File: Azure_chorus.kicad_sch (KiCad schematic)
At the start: 90 parts, among them Q1 2N5088, Q2 2N5088, Q3 2N5088, Q4 2N5088, Q5 2N5088, SW1 SW_DPDT_x2, U1 RC4558, U2 MN3207, U3 MN3102, U4 TL022

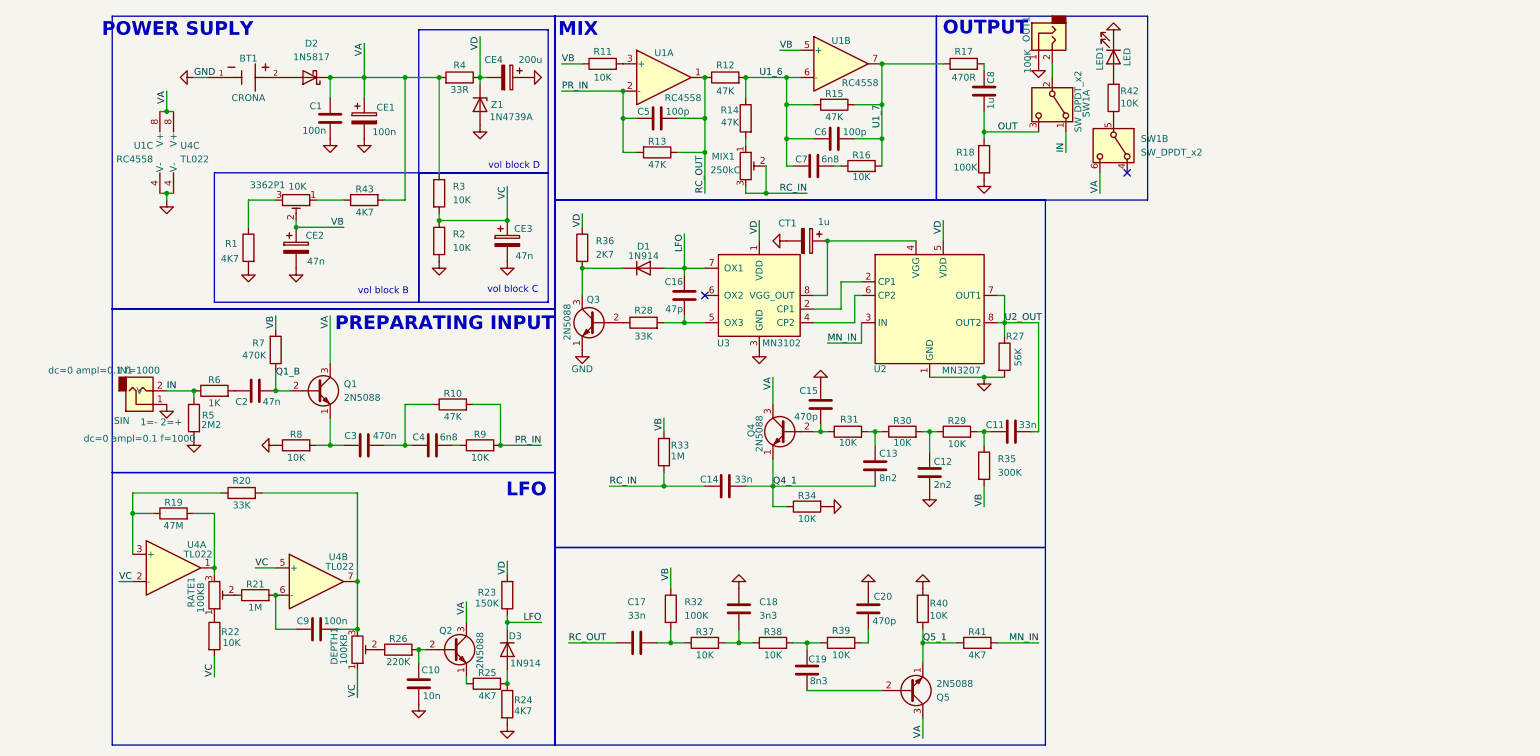
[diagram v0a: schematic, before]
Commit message: Major UPD
Schem: remade bypass, added switch to vibrato mode;

PCB: deleted old PCB, and placed firs components on new;

other: created Pr_Lib and .gitignore.
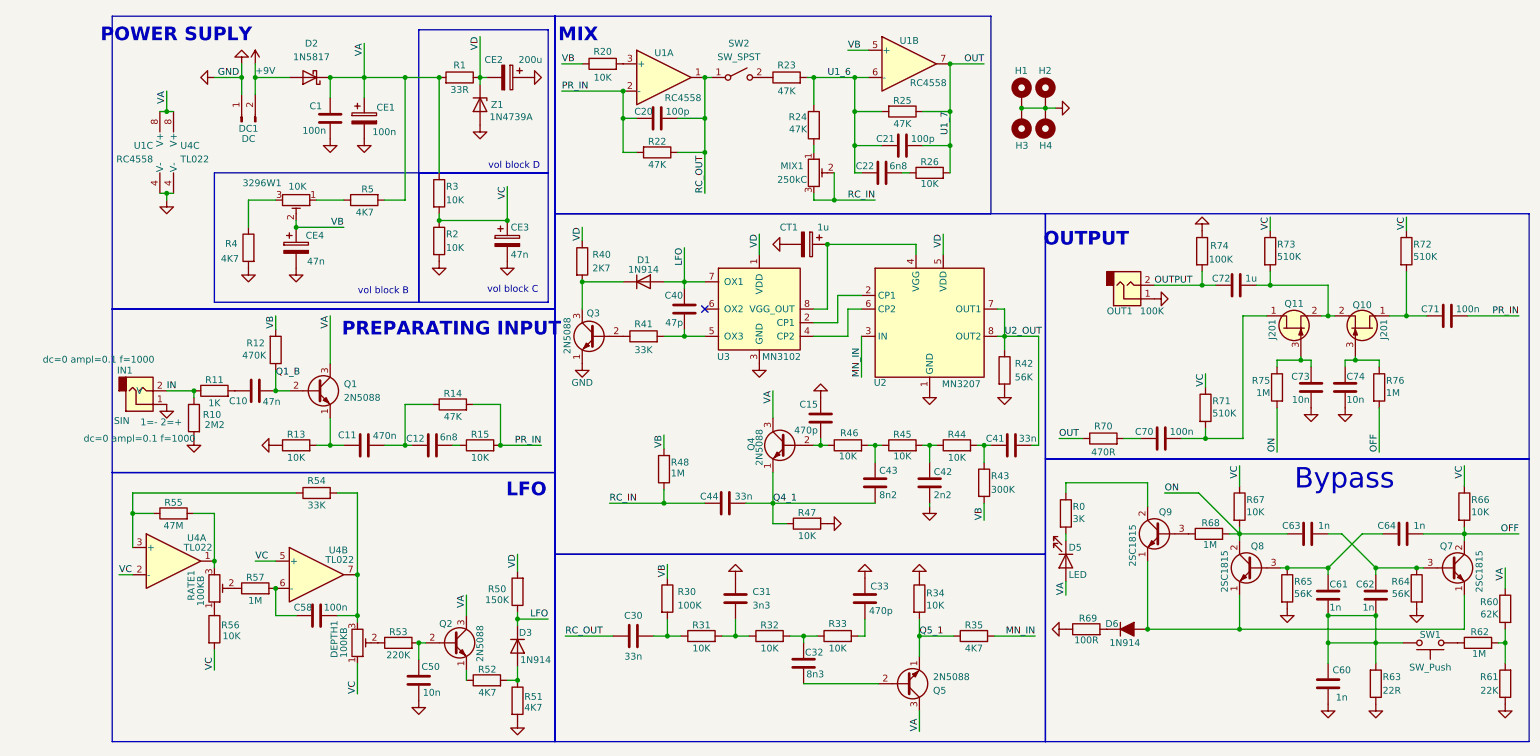
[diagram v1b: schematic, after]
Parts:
- removed BT1: CRONA, Connector_PinHeader_2.54mm:PinHeader_1x02_P2.54mm_Vertical, symbol IMP_LIB_SYM:BH23APC
- removed C8: 1u, Capacitor_THT:C_Disc_D7.0mm_W2.5mm_P5.00mm, symbol Device:C
- removed LED1: LED, LED_THT:LED_D1.8mm_W3.3mm_H2.4mm, symbol Device:LED
- removed R18: 100K, Resistor_THT:R_Axial_DIN0207_L6.3mm_D2.5mm_P7.62mm_Horizontal, symbol Device:R
- removed R42: 10K, Resistor_THT:R_Axial_DIN0207_L6.3mm_D2.5mm_P7.62mm_Horizontal, symbol Device:R
- removed SW1: SW_DPDT_x2, Button_Switch_THT:SW_NKK_GW12LJP, symbol Switch:SW_DPDT_x2
- added C60, C61, C62, C63, C64: 1n, Pr_Lib:C_Disc_D4.3_W1.9_P5.00, symbol Device:C
- added C70, C71: 100n, Pr_Lib:C_disc_D7_W2.5_P5, symbol Device:C
- added C72: 1u, Pr_Lib:C_Disc_D4.3_W1.9_P5.00, symbol Device:C
- added C73, C74: 10n, Pr_Lib:C_Disc_D4.3_W1.9_P5.00, symbol Device:C
- added D5: LED, LED_THT:LED_D3.0mm, symbol Device:LED
- added D6: 1N914, Diode_THT:D_DO-35_SOD27_P7.62mm_Horizontal, symbol PCM_Diode_AKL:1N914
- added DC1: DC, Connector_PinSocket_2.00mm:PinSocket_1x02_P2.00mm_Vertical, symbol Connector:Conn_01x02_Pin
- added H1, H2, H3, H4: MountingHole_Pad, MountingHole:MountingHole_3.2mm_M3_ISO14580_Pad, symbol Mechanical:MountingHole_Pad
- added Q10, Q11: J201, Package_TO_SOT_THT:TO-92, symbol PCM_Transistor_JFET_AKL:J201
- added Q7, Q8, Q9: 2SC1815, Package_TO_SOT_THT:TO-92_Inline, symbol Transistor_BJT:2SC1815
- added R0: 3K, Resistor_THT:R_Axial_DIN0207_L6.3mm_D2.5mm_P7.62mm_Horizontal, symbol Device:R
- added R60: 62K, Resistor_THT:R_Axial_DIN0207_L6.3mm_D2.5mm_P7.62mm_Horizontal, symbol Device:R
- added R61: 22K, Resistor_THT:R_Axial_DIN0207_L6.3mm_D2.5mm_P7.62mm_Horizontal, symbol Device:R
- added R62, R68, R75, R76: 1M, Resistor_THT:R_Axial_DIN0207_L6.3mm_D2.5mm_P7.62mm_Horizontal, symbol Device:R
- added R63: 22R, Resistor_THT:R_Axial_DIN0207_L6.3mm_D2.5mm_P7.62mm_Horizontal, symbol Device:R
- added R64, R65: 56K, Resistor_THT:R_Axial_DIN0207_L6.3mm_D2.5mm_P7.62mm_Horizontal, symbol Device:R
- added R66, R67: 10K, Resistor_THT:R_Axial_DIN0207_L6.3mm_D2.5mm_P7.62mm_Horizontal, symbol Device:R
- added R69: 100R, Resistor_THT:R_Axial_DIN0207_L6.3mm_D2.5mm_P7.62mm_Horizontal, symbol Device:R
- added R71, R72, R73: 510K, Resistor_THT:R_Axial_DIN0207_L6.3mm_D2.5mm_P7.62mm_Horizontal, symbol Device:R
- added R74: 100K, Resistor_THT:R_Axial_DIN0207_L6.3mm_D2.5mm_P7.62mm_Horizontal, symbol Device:R
- added SW1: SW_Push, Connector_PinSocket_2.00mm:PinSocket_1x02_P2.00mm_Vertical, symbol Switch:SW_Push
- added SW2: SW_SPST, Connector_PinSocket_2.00mm:PinSocket_1x02_P2.00mm_Vertical, symbol Switch:SW_SPST
- 3296W1: renamed from 3362P1; footprint MY_LIBA:POT_3362P -> Potentiometer_THT:Potentiometer_Bourns_3296W_Vertical
- C1: footprint Capacitor_THT:C_Disc_D7.0mm_W2.5mm_P5.00mm -> Pr_Lib:C_disc_D7_W2.5_P5
- C10: renamed from C2; footprint Capacitor_THT:C_Disc_D7.0mm_W2.5mm_P5.00mm -> Pr_Lib:C_Disc_D4.3_W1.9_P5.00
- C11: renamed from C3; footprint Capacitor_THT:C_Disc_D7.0mm_W2.5mm_P5.00mm -> Pr_Lib:C_disc_D7_W2.5_P5
- C12: renamed from C4; footprint Capacitor_THT:C_Disc_D7.0mm_W2.5mm_P5.00mm -> Pr_Lib:C_Disc_D4.3_W1.9_P5.00
- C15: footprint Capacitor_THT:C_Disc_D7.0mm_W2.5mm_P5.00mm -> Pr_Lib:C_Disc_D4.3_W1.9_P5.00
- C20: renamed from C5; footprint Capacitor_THT:C_Disc_D7.0mm_W2.5mm_P5.00mm -> Pr_Lib:C_Disc_D4.3_W1.9_P5.00
- C21: renamed from C6; footprint Capacitor_THT:C_Disc_D7.0mm_W2.5mm_P5.00mm -> Pr_Lib:C_Disc_D4.3_W1.9_P5.00
- C22: renamed from C7; footprint Capacitor_THT:C_Disc_D7.0mm_W2.5mm_P5.00mm -> Pr_Lib:C_Disc_D4.3_W1.9_P5.00
- C30: renamed from C17; footprint Capacitor_THT:C_Disc_D7.0mm_W2.5mm_P5.00mm -> Pr_Lib:C_Disc_D4.3_W1.9_P5.00
- C31: renamed from C18; footprint Capacitor_THT:C_Disc_D7.0mm_W2.5mm_P5.00mm -> Pr_Lib:C_Disc_D4.3_W1.9_P5.00
- C32: renamed from C19; footprint Capacitor_THT:C_Disc_D7.0mm_W2.5mm_P5.00mm -> Pr_Lib:C_Disc_D4.3_W1.9_P5.00
- C33: renamed from C20; footprint Capacitor_THT:C_Disc_D7.0mm_W2.5mm_P5.00mm -> Pr_Lib:C_Disc_D4.3_W1.9_P5.00
- C40: renamed from C16; footprint Capacitor_THT:C_Disc_D7.0mm_W2.5mm_P5.00mm -> Pr_Lib:C_Disc_D4.3_W1.9_P5.00
- C41: renamed from C11; footprint Capacitor_THT:C_Disc_D7.0mm_W2.5mm_P5.00mm -> Pr_Lib:C_Disc_D4.3_W1.9_P5.00
- C42: renamed from C12; footprint Capacitor_THT:C_Disc_D7.0mm_W2.5mm_P5.00mm -> Pr_Lib:C_Disc_D4.3_W1.9_P5.00
- C43: renamed from C13; footprint Capacitor_THT:C_Disc_D7.0mm_W2.5mm_P5.00mm -> Pr_Lib:C_Disc_D4.3_W1.9_P5.00
- C44: renamed from C14; footprint Capacitor_THT:C_Disc_D7.0mm_W2.5mm_P5.00mm -> Pr_Lib:C_Disc_D4.3_W1.9_P5.00
- C50: renamed from C10; footprint Capacitor_THT:C_Disc_D7.0mm_W2.5mm_P5.00mm -> Pr_Lib:C_Disc_D4.3_W1.9_P5.00
- C58: renamed from C9; footprint Capacitor_THT:C_Disc_D7.0mm_W2.5mm_P5.00mm -> Pr_Lib:C_disc_D7_W2.5_P5
- CE1: footprint Capacitor_THT:CP_Radial_D6.3mm_P2.50mm -> Capacitor_THT:CP_Radial_D4.0mm_P1.50mm
- CE3: footprint Capacitor_THT:CP_Radial_D5.0mm_P2.50mm -> Capacitor_THT:CP_Radial_D4.0mm_P1.50mm
- CE4: renamed from CE2; footprint Capacitor_THT:CP_Radial_D5.0mm_P2.50mm -> Capacitor_THT:CP_Radial_D4.0mm_P1.50mm
- DEPTH1, MIX1, RATE1: footprint Connector_PinHeader_2.54mm:PinHeader_1x03_P2.54mm_Vertical -> Package_TO_SOT_THT:TO-92S
- IN1, OUT1: footprint Connector_PinHeader_2.54mm:PinHeader_1x02_P2.54mm_Vertical -> Connector_PinHeader_2.00mm:PinHeader_1x02_P2.00mm_Vertical
- Q1, Q2, Q3, Q4, Q5: footprint Package_TO_SOT_THT:TO-92_Inline_Wide -> Package_TO_SOT_THT:TO-92_Inline
- renumbered CE4 to CE2, R4 to R1, R5 to R10, R6 to R11, R7 to R12, R8 to R13, R10 to R14, R9 to R15, R11 to R20, R13 to R22, R12 to R23, R14 to R24, R15 to R25, R16 to R26, R32 to R30, R37 to R31, R38 to R32, R39 to R33, R40 to R34, R41 to R35, R1 to R4, R36 to R40, R28 to R41, R27 to R42, R35 to R43, R29 to R44, R30 to R45, R31 to R46, R34 to R47, R33 to R48, R43 to R5, R23 to R50, R24 to R51, R25 to R52, R26 to R53, R20 to R54, R19 to R55, R22 to R56, R21 to R57, R17 to R70
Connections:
- net U1_7 is gone; now on net OUT: C21.2, R25.1, R26.2, R70.1, U1.7
- net GND: now also C60.2, C73.1, C74.1, DC1.1 (Pin_1), H1.1, H2.1, H3.1, H4.1, R61.1, R63.1, R64.2, R65.2, R69.1, R74.1
- net PR_IN: now also C71.2
- net RC_OUT: now also SW2.1 (A); no longer R23.1
- net VA: now also D5.2 (A), R60.1
- net VC: now also R66.1, R67.1, R71.1, R72.1, R73.1
- net at R70.2: now also C70.1
- net OUTPUT: now reaches OUT1.2
- net OUTPUT: now also C72.1, R74.2
- net +9V: now reaches D2.2 (A)
- net +9V: now also DC1.2 (Pin_2)
- new net: C71.1, Q10.1 (D), R72.2
- new net: C72.2, Q10.2 (S), Q11.2 (S), R73.2
- new net: C74.2, Q10.3 (G), R76.1
- new net: C61.2, C64.1, Q8.3 (B), R65.1
- new net: D6.2 (A), Q7.1 (E), Q8.1 (E), Q9.1 (E)
- new net: C62.2, C63.2, Q7.3 (B), R64.1
- new net: R62.1, SW1.1
- new net: C60.1, C61.1, C62.1, R63.2, SW1.2
- new net: D5.1 (K), R0.2
- new net: Q9.2 (C), R0.1
- new net: Q9.3 (B), R68.1
- new net: C70.2, Q11.1 (D), R71.2
- new net: R23.1, SW2.2 (B)
- new net: R60.2, R61.2, R62.2
- new net: C73.2, Q11.3 (G), R75.1
- new net: D6.1 (K), R69.2
- new net OFF: C64.2, Q7.2 (C), R66.2, R76.2
- new net ON: C63.1, Q8.2 (C), R67.2, R68.2, R75.2
- no-connect marks 2 -> 1
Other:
- note added: "Bypass"
- moved on the sheet: C15, C21, C22, C30, C31, C32, C33, C40, C41, C42, C43, C44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
